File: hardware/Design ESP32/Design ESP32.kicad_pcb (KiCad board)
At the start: 2 copper layers, 6 parts, among them U1 ESP32-S3-WROOM-1, U2 AMS1117-3.3

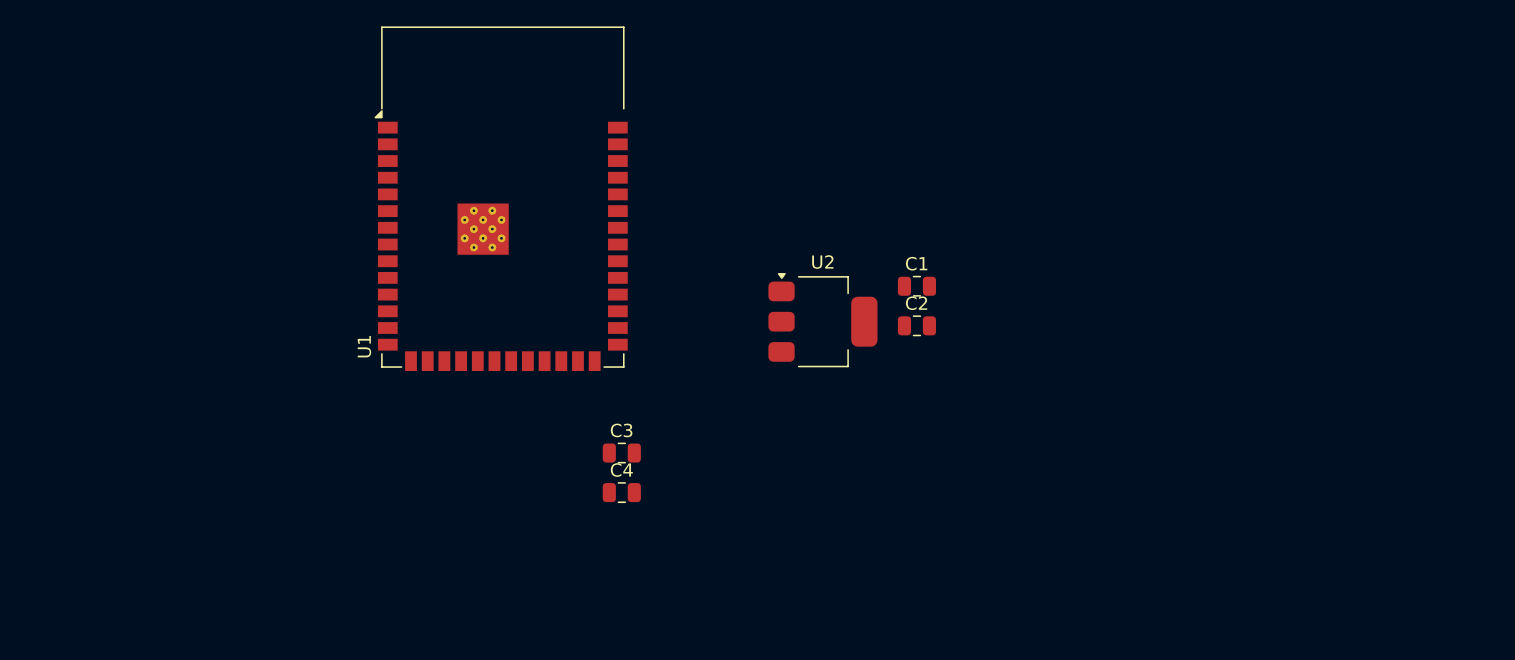
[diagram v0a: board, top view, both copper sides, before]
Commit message: crosscheck schenmatic, progres track pcb
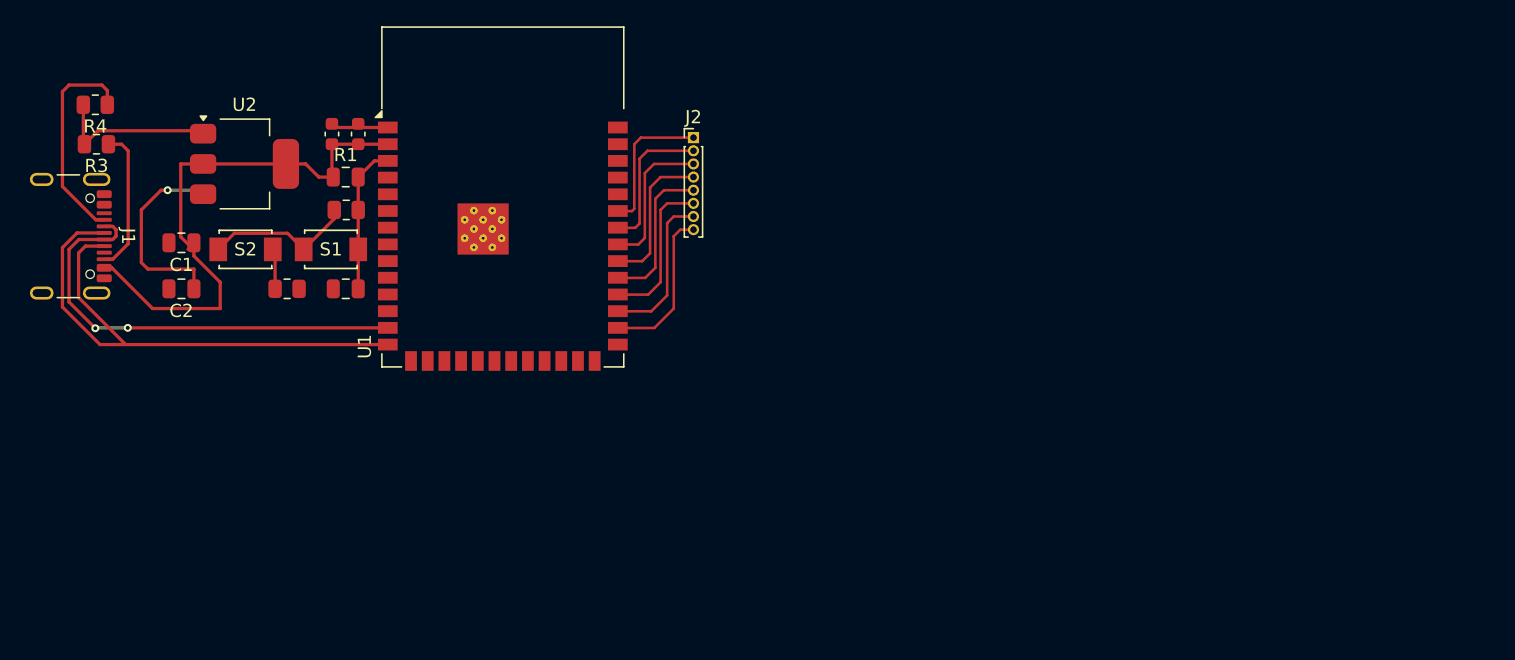
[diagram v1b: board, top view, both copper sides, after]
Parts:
- added C5: 1uF, Resistor_SMD:R_0805_2012Metric, F.Cu at (126.1, 83.0)
- added C6: 100nF, Capacitor_SMD:C_0805_2012Metric, F.Cu at (126.0, 89.0)
- added J1: USB_C_Receptacle_USB2.0_16P, Connector_USB:USB_C_Receptacle_GCT_USB4105-xx-A_16P_TopMnt_Horizontal, F.Cu at (104.0, 85.0)
- added J2: Conn_01x08_Pin, Connector_PinHeader_1.00mm:PinHeader_1x08_P1.00mm_Vertical, F.Cu at (152.5, 77.5)
- added R1: 10K, Capacitor_SMD:C_0805_2012Metric, F.Cu at (126.0, 80.5)
- added R2: 100R, Resistor_SMD:R_0805_2012Metric, F.Cu at (121.6, 89.0)
- added R3: 5.1K, Resistor_SMD:R_0805_2012Metric, F.Cu at (107.1, 78.0)
- added R4: 5.1K, Resistor_SMD:R_0805_2012Metric, F.Cu at (107.0, 75.0)
- added S1: TS-1088-AR02016, TS-1088-AR02016:SW_TS-1088-AR02016, F.Cu at (124.9, 86.0)
- added S2: TS-1088-AR02016, TS-1088-AR02016:SW_TS-1088-AR02016, F.Cu at (118.4, 86.0)
- C3, C4: footprint Capacitor_SMD:C_0805_2012Metric -> Capacitor_SMD:C_0603_1608Metric
- moved C1 56.0 mm to (113.5, 85.5), turned to 180 degrees
- moved C2 56.0 mm to (113.5, 89.0), turned to 180 degrees
- moved U2 45.6 mm to (118.3, 79.5)
- moved C4 33.9 mm to (127.0, 77.2), turned to 90 degrees
- moved C3 32.8 mm to (125.0, 77.2), turned to 90 degrees
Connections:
- U1 pad 13: unconnected-(U1-USB_D--Pad13) -> D-
- U1 pad 14: unconnected-(U1-USB_D+-Pad14) -> D+
- U1 pad 28: unconnected-(U1-IO35-Pad28) -> Net-(J2-Pin_8)
- U1 pad 29: unconnected-(U1-IO36-Pad29) -> Net-(J2-Pin_7)
- U1 pad 3: unconnected-(U1-EN-Pad3) -> EN
- U1 pad 30: unconnected-(U1-IO37-Pad30) -> Net-(J2-Pin_6)
- U1 pad 31: unconnected-(U1-IO38-Pad31) -> Net-(J2-Pin_5)
- U1 pad 32: unconnected-(U1-IO39-Pad32) -> Net-(J2-Pin_4)
- U1 pad 33: unconnected-(U1-IO40-Pad33) -> Net-(J2-Pin_3)
- U1 pad 34: unconnected-(U1-IO41-Pad34) -> Net-(J2-Pin_2)
- U1 pad 35: unconnected-(U1-IO42-Pad35) -> Net-(J2-Pin_1)
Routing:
- net D+: track 0.00 -> 44.7 mm
- net +3V3: track 0.00 -> 41.8 mm
- net D-: track 0.00 -> 34.7 mm, vias 0 -> 2
- net GND: track 0.00 -> 28.4 mm
- net Net-(J1-CC1): track 0.00 -> 16.3 mm
- net +5V: track 0.00 -> 15.0 mm, vias 0 -> 1
- net Net-(J2-Pin_8): track 0.00 -> 12.1 mm
- net Net-(J2-Pin_7): track 0.00 -> 12.0 mm
- net Net-(J2-Pin_6): track 0.00 -> 11.8 mm
- net Net-(J2-Pin_5): track 0.00 -> 11.6 mm
- net Net-(J2-Pin_4): track 0.00 -> 11.3 mm
- net EN: track 0.00 -> 11.3 mm
- net Net-(J2-Pin_3): track 0.00 -> 11.2 mm
- net Net-(J1-CC2): track 0.00 -> 11.1 mm
- net Net-(J2-Pin_2): track 0.00 -> 11.1 mm
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
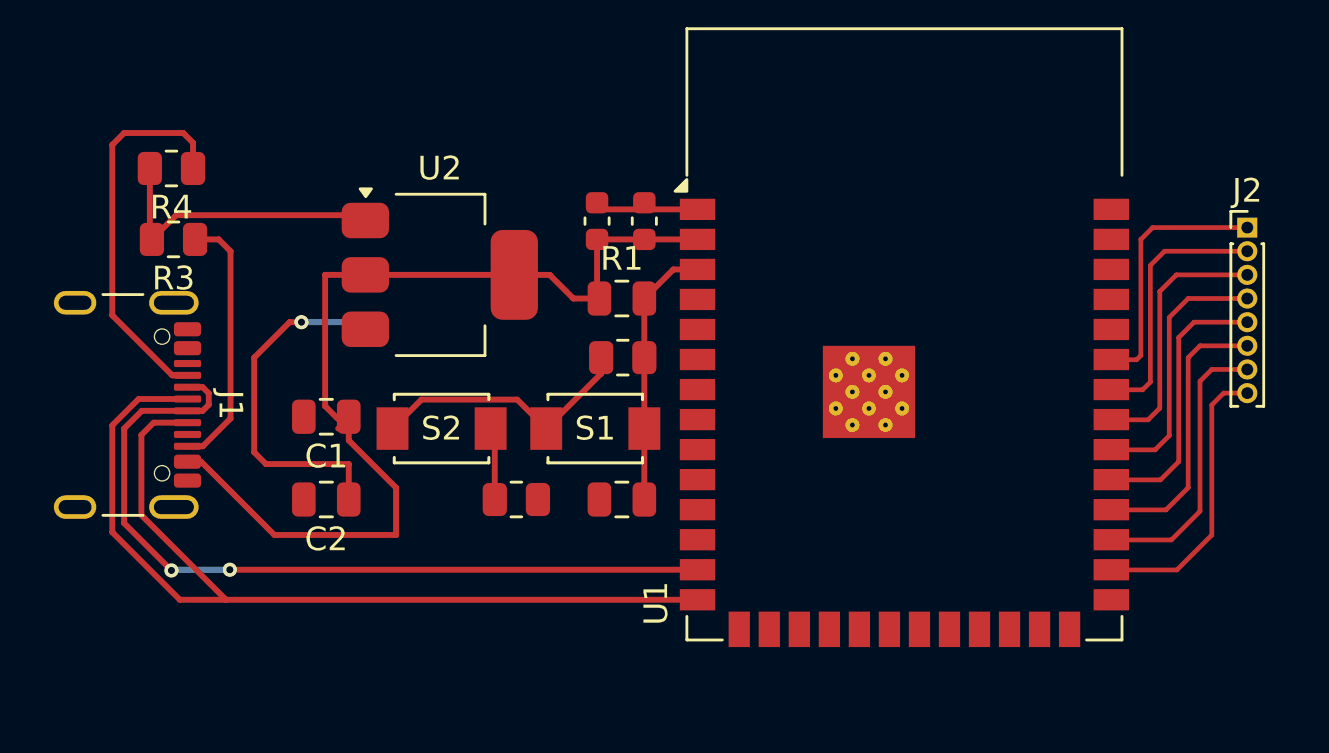
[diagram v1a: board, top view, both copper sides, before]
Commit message: jalur pcb, penanganan error 36 to 11
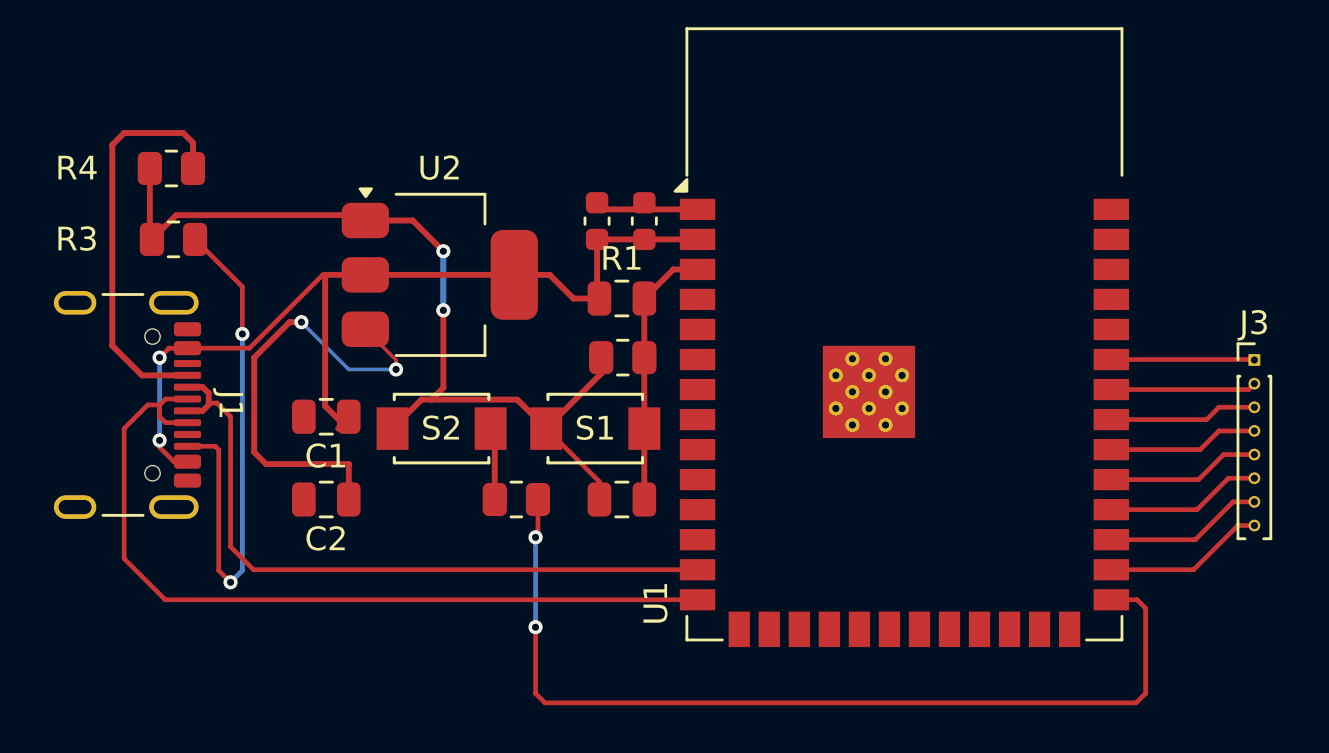
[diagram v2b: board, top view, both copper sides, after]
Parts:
- removed J2: Conn_01x08_Pin, Connector_PinHeader_1.00mm:PinHeader_1x08_P1.00mm_Vertical
- added J3: Conn_01x08_Pin, Connector_PinHeader_1.00mm:PinHeader_1x08_P1.00mm_Vertical, F.Cu at (152.8, 83.1)
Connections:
- U1 pad 27: unconnected-(U1-IO0-Pad27) -> BOOT
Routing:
- net BOOT: track 0.00 -> 39.6 mm, vias 0 -> 2
- net GND: track 28.4 -> 42.7 mm, vias 0 -> 2
- net Net-(J1-CC2): track 11.1 -> 22.7 mm, vias 0 -> 2
- net D+: track 44.7 -> 35.5 mm
- net D-: track 34.7 -> 29.3 mm, vias 2 -> 0
- net Net-(J3-Pin_8): track 12.1 -> 6.82 mm
- net Net-(J3-Pin_7): track 12.0 -> 6.71 mm
- net Net-(J3-Pin_6): track 11.8 -> 6.60 mm
- net Net-(J3-Pin_5): track 11.6 -> 6.49 mm
- net Net-(J3-Pin_4): track 11.3 -> 6.38 mm
- net Net-(J3-Pin_2): track 11.1 -> 6.15 mm
- net Net-(J3-Pin_3): track 11.2 -> 6.27 mm
- net Net-(J3-Pin_1): track 10.9 -> 6.06 mm
- net +5V: track 15.0 -> 19.4 mm, vias 1 -> 2
- net +3V3: track 41.8 -> 39.6 mm, vias 0 -> 2
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
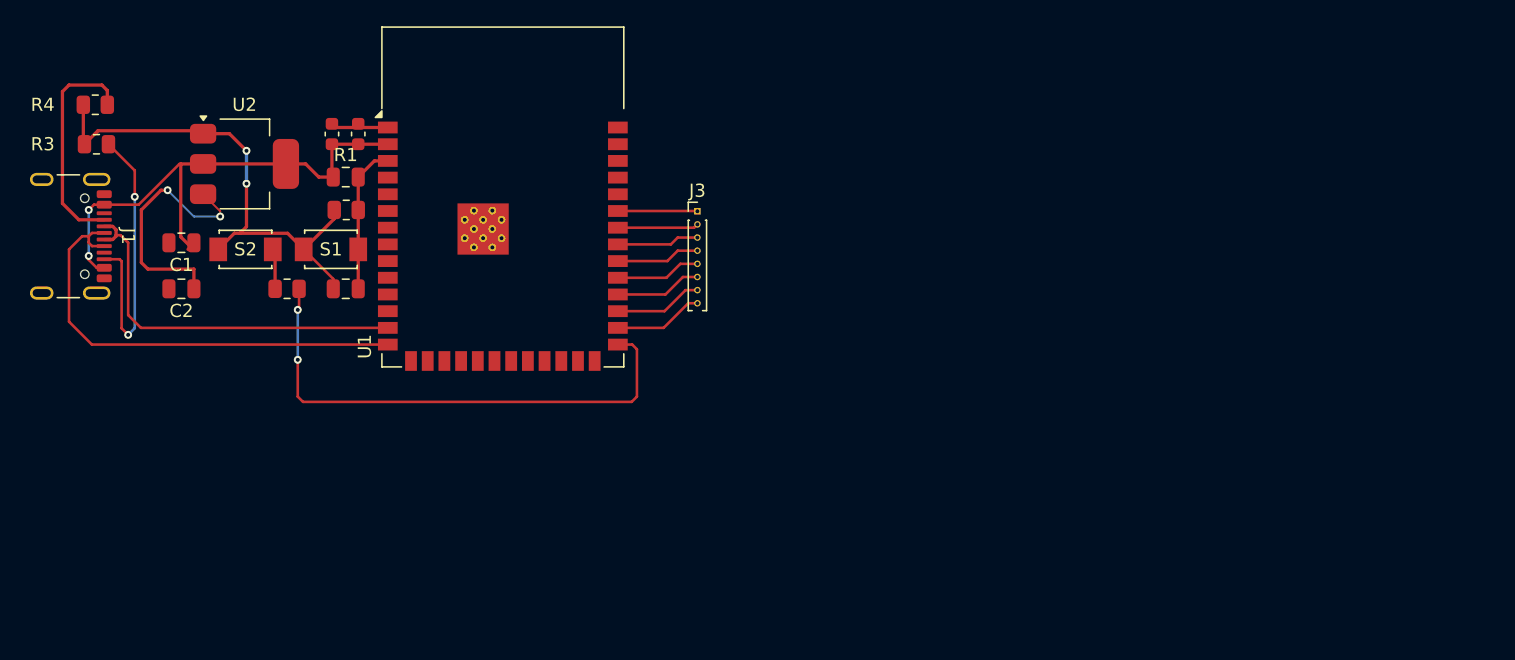
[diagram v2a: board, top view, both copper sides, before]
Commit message: lanjut penanganan error dan penyelesaian design ESP32
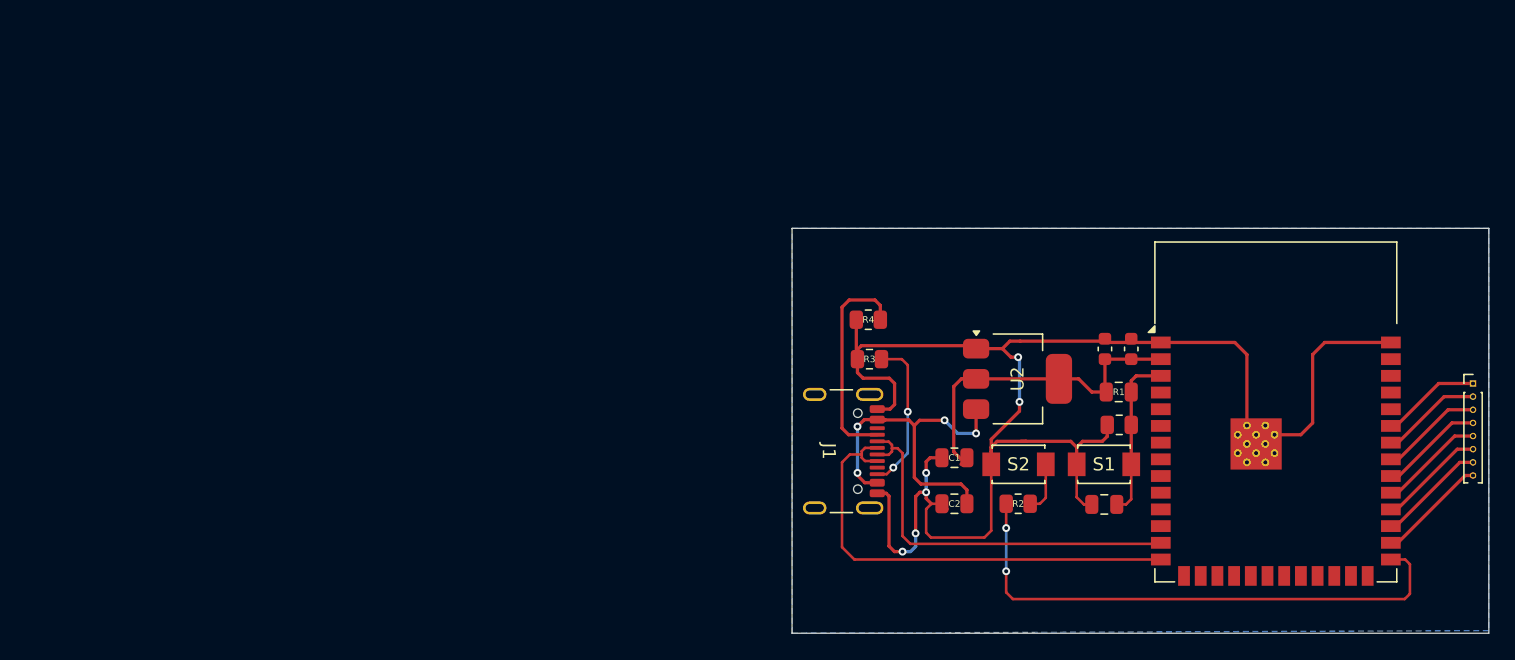
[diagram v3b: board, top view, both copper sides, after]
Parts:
- moved C3 61.0 mm to (183.8, 93.6)
- moved C4 61.0 mm to (185.8, 93.6)
- moved J1 61.0 mm to (162.8, 101.3)
- moved R4 61.0 mm to (165.8, 91.3)
- moved U1 61.0 mm to (196.8, 98.3)
- moved U2 61.0 mm to (177.2, 95.8)
- moved C1 61.0 mm to (172.3, 101.8)
- moved C2 61.0 mm to (172.3, 105.3)
- moved R1 61.0 mm to (184.8, 96.8)
- moved S1 61.0 mm to (183.7, 102.3)
- moved S2 61.0 mm to (177.2, 102.3)
- moved C5 61.0 mm to (184.9, 99.3)
- moved R3 61.0 mm to (165.9, 94.3)
- moved J3 60.4 mm to (211.8, 96.2)
- moved C6 60.0 mm to (183.8, 105.4)
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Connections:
- J1 pad A1: unconnected-(J1-GND-PadA1)_1 -> GND
- J1 pad A12: unconnected-(J1-GND-PadA1)_2 -> GND
- J1 pad A4: +3V3 -> +5V
- J1 pad A9: +3V3 -> +5V
- J1 pad B1: unconnected-(J1-GND-PadA1) -> GND
- J1 pad B12: unconnected-(J1-GND-PadA1)_3 -> GND
- J1 pad B4: +3V3 -> +5V
- J1 pad B9: +3V3 -> +5V
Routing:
- net GND: track 42.7 -> 119.4 mm, vias 2 -> 6
- net +3V3: track 39.6 -> 25.6 mm, vias 2 -> 0
- net Net-(J1-CC2): track 22.7 -> 12.0 mm
- net +5V: track 19.4 -> 26.7 mm, vias 2 -> 4
- net BOOT: track 39.6 -> 41.7 mm
- net Net-(J3-Pin_8): track 6.82 -> 8.37 mm
- net Net-(J3-Pin_5): track 6.49 -> 8.04 mm
- net Net-(J3-Pin_2): track 6.15 -> 7.70 mm
- net Net-(J3-Pin_4): track 6.38 -> 7.92 mm
- net Net-(J3-Pin_6): track 6.60 -> 8.15 mm
- net Net-(J3-Pin_3): track 6.27 -> 7.81 mm
- net Net-(J3-Pin_7): track 6.71 -> 8.26 mm
- net Net-(J3-Pin_1): track 6.06 -> 7.59 mm
- net EN: track 11.3 -> 12.7 mm
- net Net-(R2-Pad2): track 3.07 -> 4.17 mm
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- added copper zone on B.Cu, net GND
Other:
- board outline added: 53 x 30.8 mm
